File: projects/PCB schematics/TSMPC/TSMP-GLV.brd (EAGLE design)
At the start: 39.4 x 32.7 mm, 2 parts, among them X1 5566-6, X2 5566-2

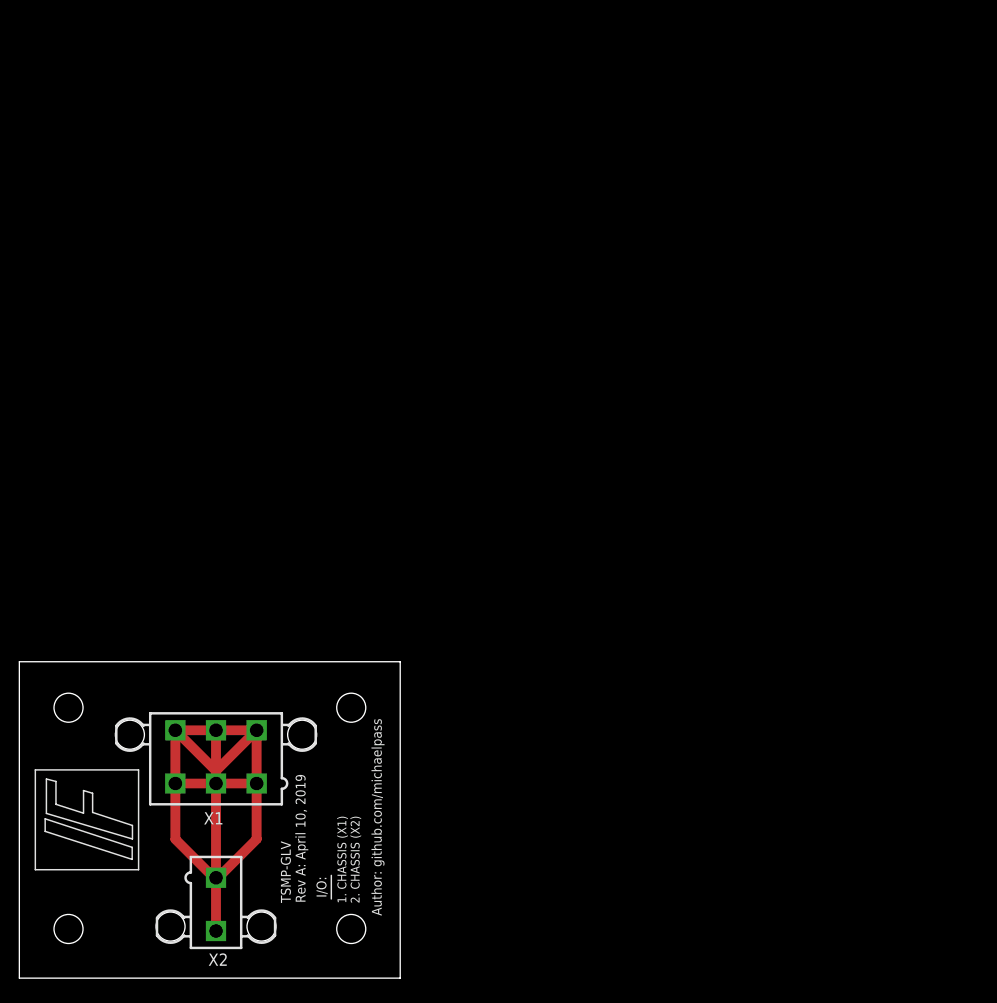
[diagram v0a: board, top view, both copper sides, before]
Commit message: TSMPC - Board 3900milx3900mil redo.
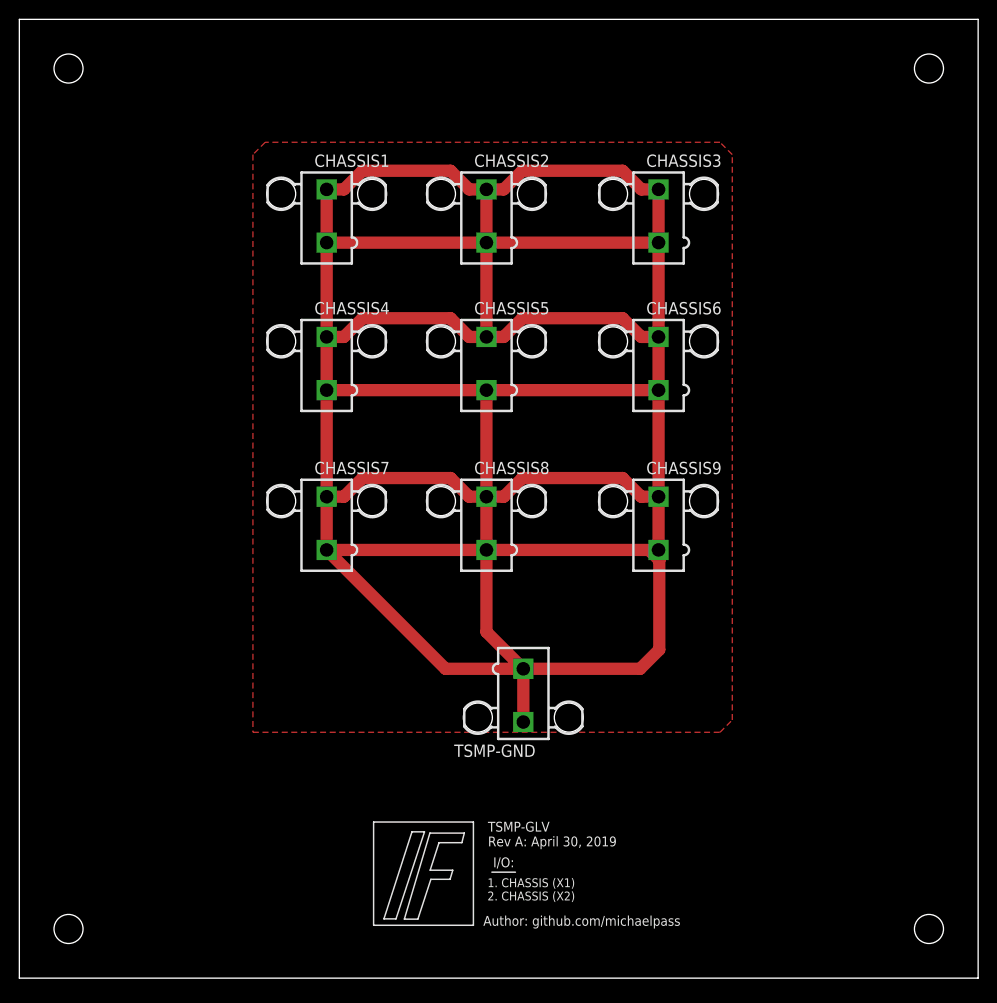
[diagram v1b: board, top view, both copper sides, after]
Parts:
- removed X1: 5566-6, con-molex:5566-6
- removed X2: 5566-2, con-molex:5566-2
- added CHASSIS1, CHASSIS2, CHASSIS3, CHASSIS4, CHASSIS5, CHASSIS6, CHASSIS7, CHASSIS8, CHASSIS9, TSMP-GND: 5566-2, con-molex:5566-2
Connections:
- net GND: now also CHASSIS1.1, CHASSIS1.2, CHASSIS2.1, CHASSIS2.2, CHASSIS3.1, CHASSIS3.2, CHASSIS4.1, CHASSIS4.2, CHASSIS5.1, CHASSIS5.2, CHASSIS6.1, CHASSIS6.2, CHASSIS7.1, CHASSIS7.2, CHASSIS8.1, CHASSIS8.2, CHASSIS9.1, CHASSIS9.2, TSMP-GND.1, TSMP-GND.2; no longer X1.1, X1.2, X1.3, X1.4, X1.5, X1.6, X2.1, X2.2
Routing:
- net GND: track 83.8 -> 392.3 mm
- added copper zone on layer 1, net GND
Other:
- board size 39.4 x 32.7 mm -> 99.1 x 99.1 mm
- board text added: "TSMP-GLV Rev A: April 30, 2019"
- board text removed: "TSMP-GLV Rev A: April 10, 2019"

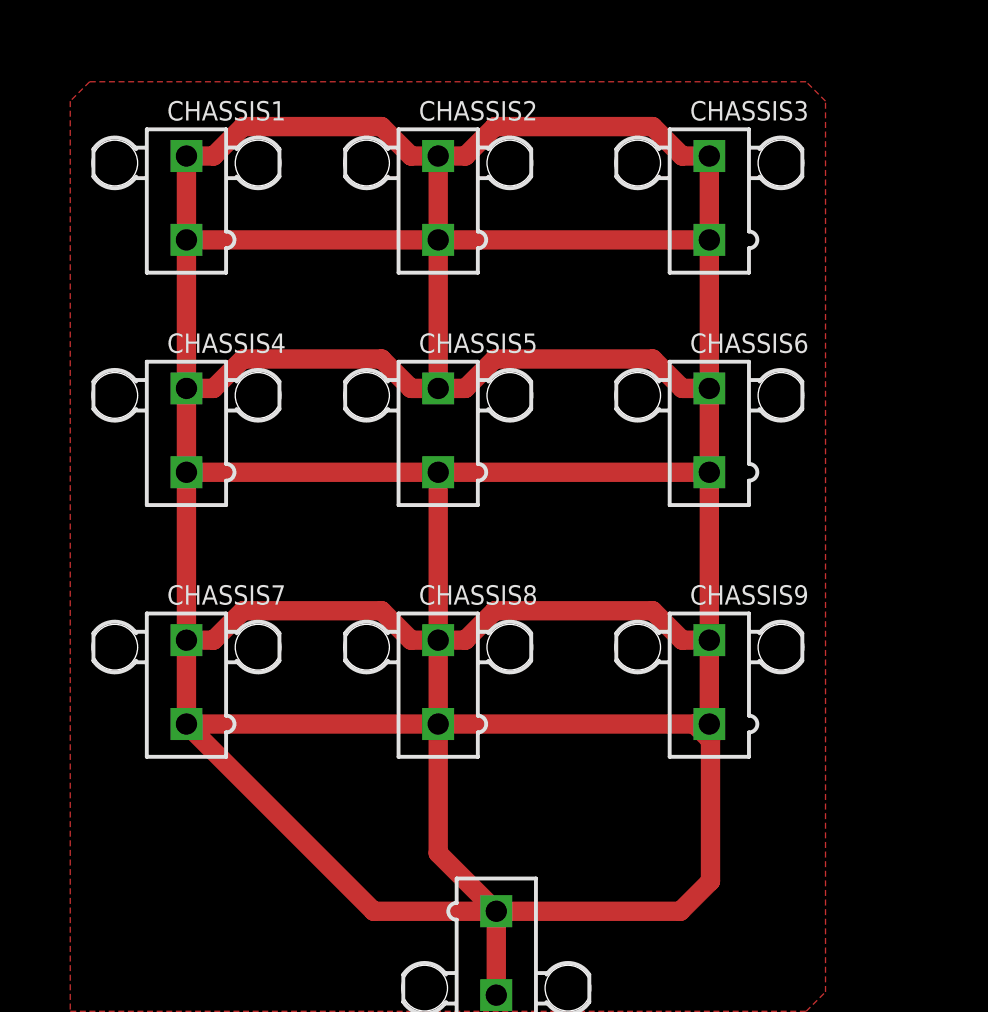
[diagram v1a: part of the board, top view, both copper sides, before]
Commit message: ACCUM - Added IMD fuses.
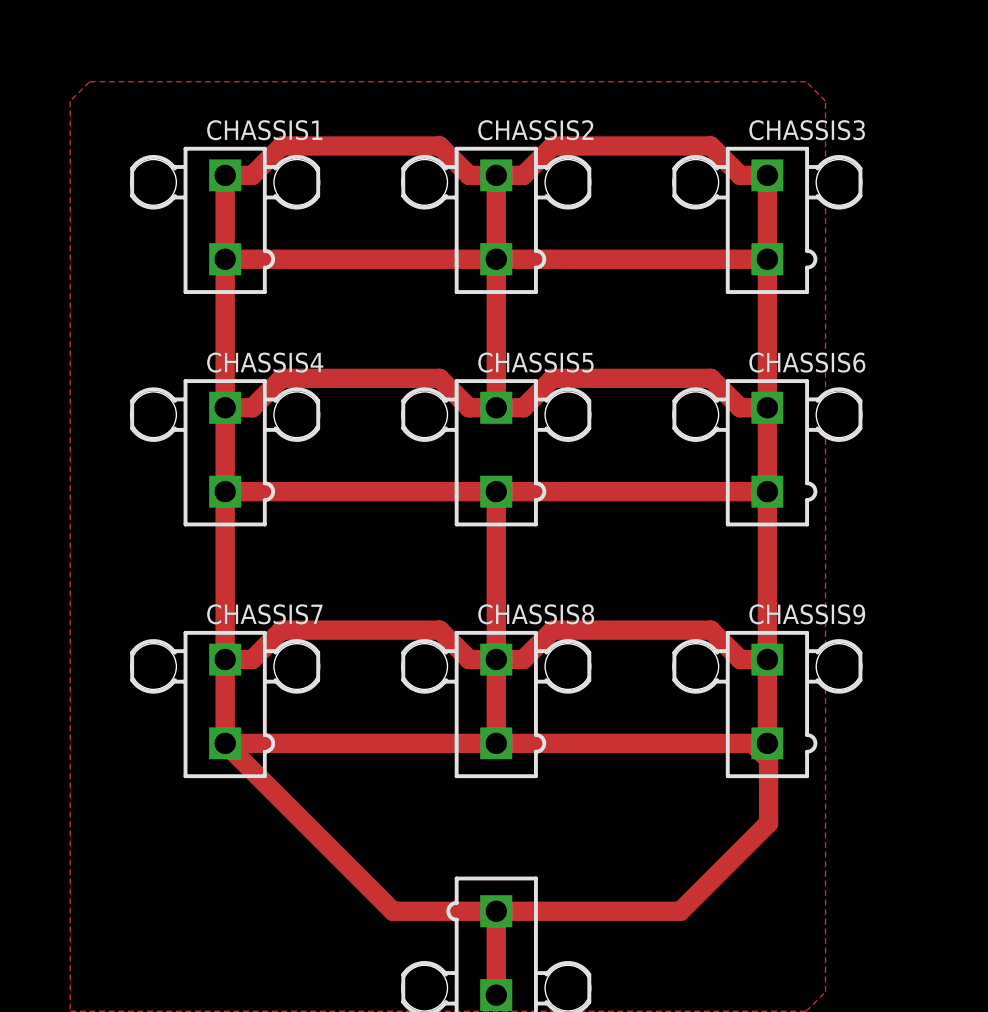
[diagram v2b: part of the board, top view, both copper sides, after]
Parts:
- moved CHASSIS5 4.02 mm to (52.1, 62.2)
- moved CHASSIS8 4.02 mm to (52.1, 45.7)
- moved CHASSIS2 4.02 mm to (52.1, 77.5)
- moved CHASSIS6 4.02 mm to (69.8, 62.2)
- moved CHASSIS9 4.02 mm to (69.8, 45.7)
- moved CHASSIS3 4.02 mm to (69.8, 77.5)
- moved CHASSIS4 2.84 mm to (34.3, 62.2)
- moved CHASSIS7 2.84 mm to (34.3, 45.7)
- moved CHASSIS1 2.84 mm to (34.3, 77.5)
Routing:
- net GND: track 392.3 -> 383.3 mm

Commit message: PROJ - Gerber files major milestone - 05/05/19.
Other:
- board text added: "TSMP-GLV Rev A: May 5th, 2019"
- board text removed: "TSMP-GLV Rev A: April 30, 2019"
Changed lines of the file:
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@@
 <wire x1="45.974" y1="14.986" x2="42.418" y2="14.986" width="0.1524" layer="25"/>
 <text x="48.4124" y="13.6144" size="1.016" layer="25" font="vector">TSMP-GLV
-Rev A: April 30, 2019</text>
+Rev A: May 5th, 2019</text>
 <text x="47.9298" y="5.4102" size="1.016" layer="25" font="vector">Author: github.com/michaelpass</text>
 <text x="48.9458" y="11.4554" size="1.016" layer="25" font="vector">I/O:</text>
@@
 <wire x1="69.85" y1="59.48" x2="52.07" y2="59.48" width="1.27" layer="1"/>
 <wire x1="34.29" y1="59.48" x2="34.29" y2="48.47" width="1.27" layer="1"/>
-<wire x1="34.29" y1="48.26" x2="34.29" y2="48.47" width="1.27" layer="1"/>
 <wire x1="34.29" y1="48.47" x2="34.29" y2="42.97" width="1.27" layer="1"/>
 <wire x1="34.29" y1="42.97" x2="45.3" y2="31.96" width="1.27" layer="1"/>
@@
 <wire x1="52.07" y1="42.97" x2="68.8662" y2="42.97" width="1.27" layer="1"/>
 <wire x1="68.8662" y1="42.97" x2="69.9262" y2="41.91" width="1.27" layer="1"/>
-<wire x1="52.07" y1="42.97" x2="34.29" y2="42.97" width="1.27" layer="1"/>
 <wire x1="52.07" y1="42.97" x2="52.07" y2="48.47" width="1.27" layer="1"/>
 <wire x1="52.07" y1="48.47" x2="52.07" y2="59.48" width="1.27" layer="1"/>
@@
 <vertex x="25.4" y="86.36"/>
 </polygon>
-<wire x1="52.07" y1="74.72" x2="34.29" y2="74.72" width="0" layer="19"/>
-<wire x1="52.07" y1="59.48" x2="34.29" y2="59.48" width="0" layer="19"/>
-<wire x1="34.29" y1="42.97" x2="52.07" y2="42.97" width="0" layer="19"/>
+<wire x1="34.29" y1="42.97" x2="52.07" y2="42.97" width="1.27" layer="1"/>
 </signal>
 </signals>
